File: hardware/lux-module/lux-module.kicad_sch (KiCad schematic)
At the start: 5 parts, among them J1 Conn_01x04, U1 TSL25911FN

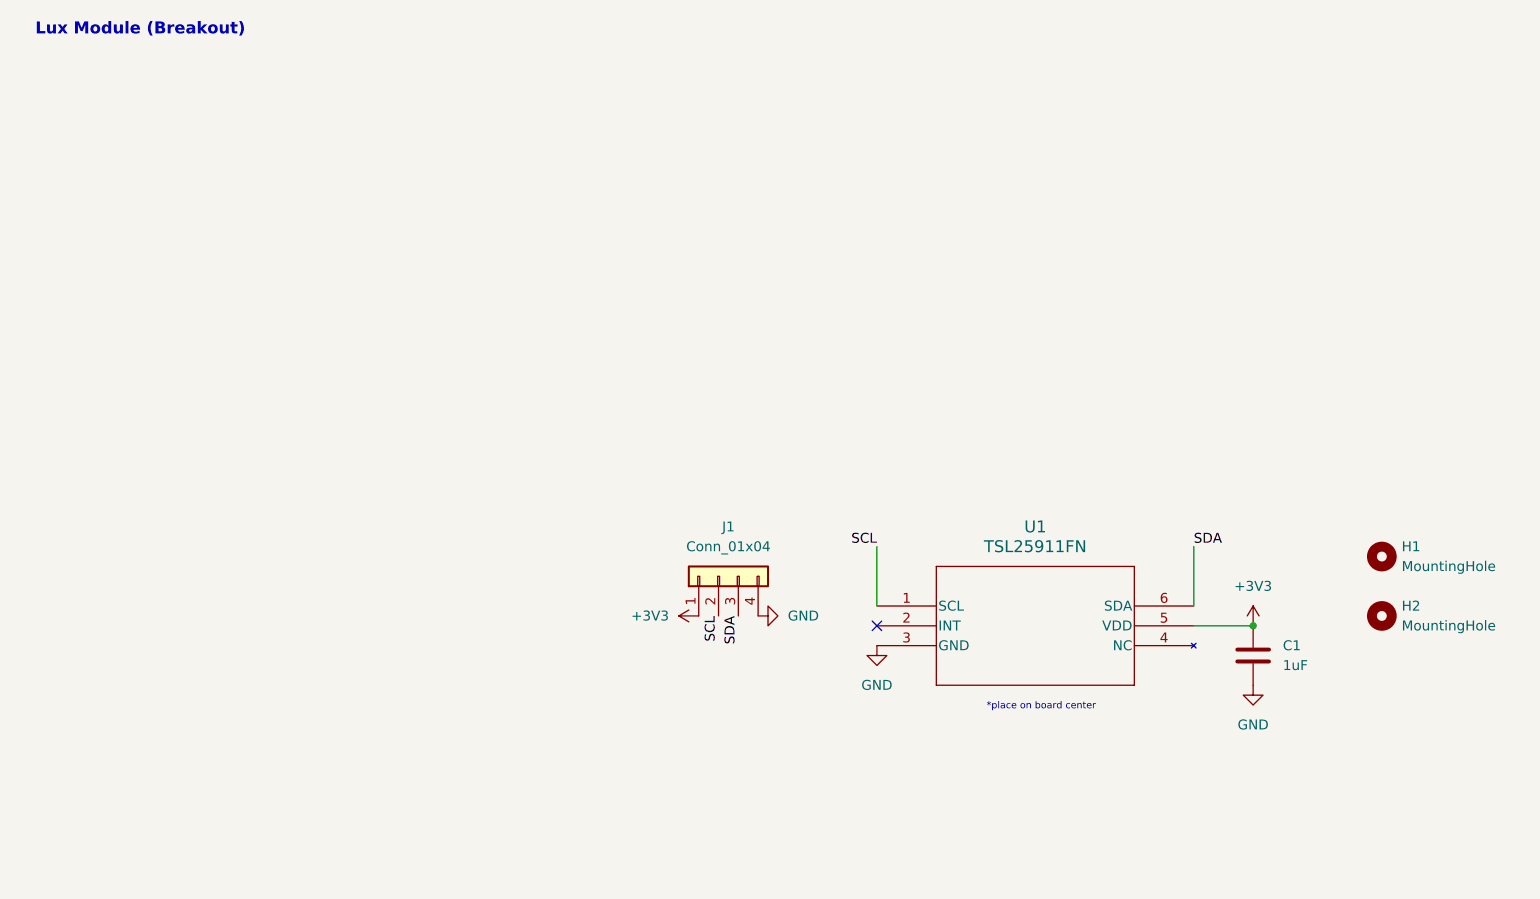
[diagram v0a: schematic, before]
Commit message: finish lux moudle/ALS
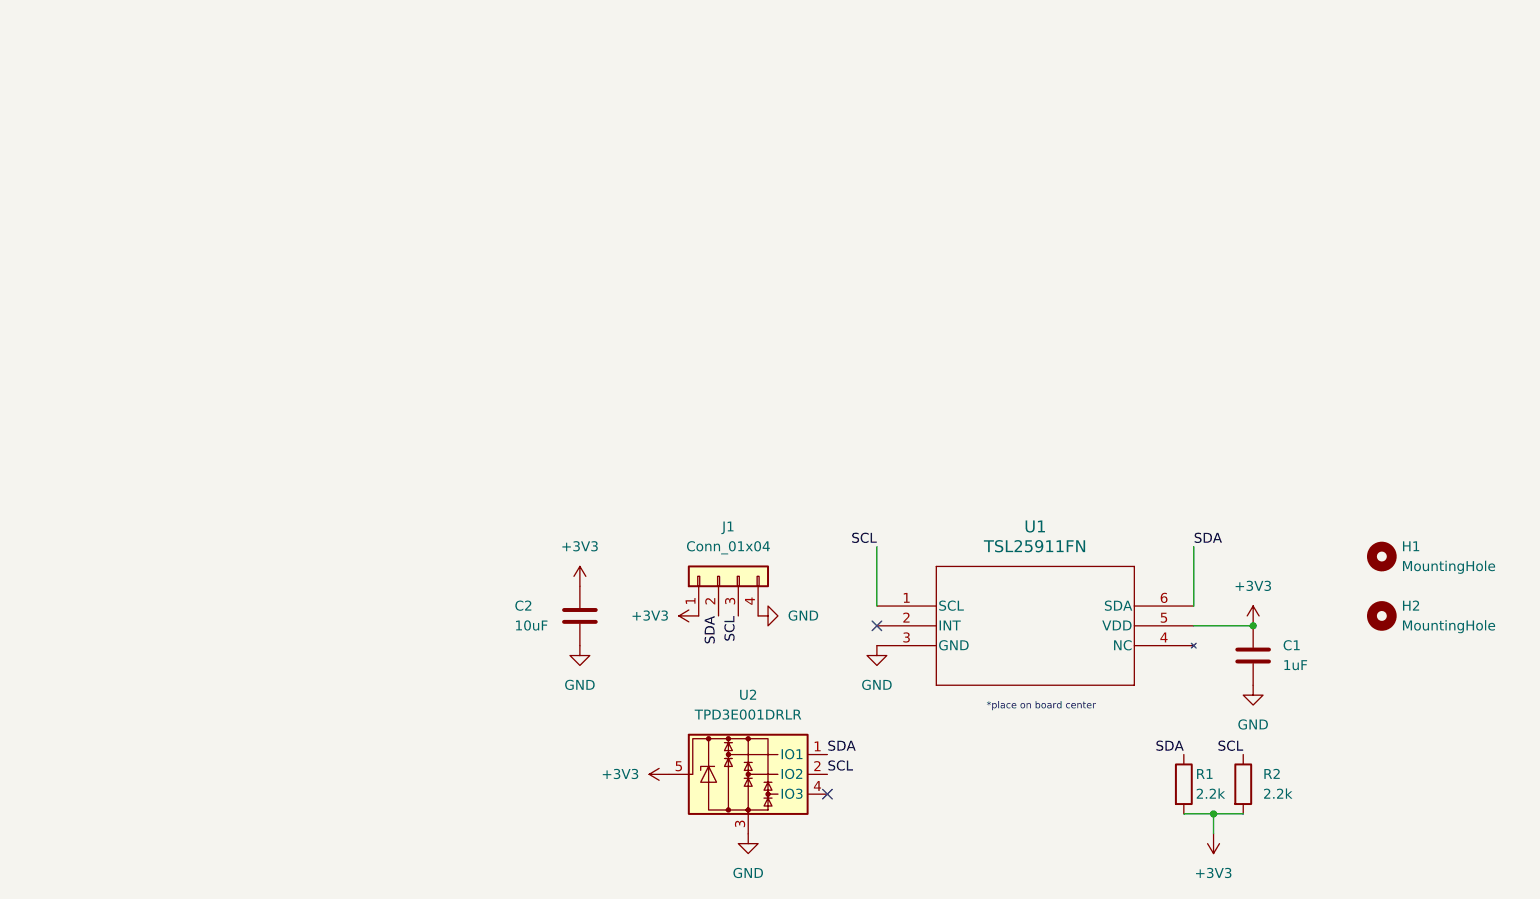
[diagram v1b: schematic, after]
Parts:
- added C2: 10uF, Capacitor_SMD:C_0402_1005Metric, symbol Device:C
- added R1, R2: 2.2k, Resistor_SMD:R_0402_1005Metric, symbol Device:R
- added U2: TPD3E001DRLR, Package_TO_SOT_SMD:SOT-553, symbol Power_Protection:TPD3E001DRLR
- C1: footprint Capacitor_SMD:C_0603_1608Metric -> Capacitor_SMD:C_0402_1005Metric
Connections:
- net +3V3: now also C2.1, R1.2, R2.2, U2.5
- net GND: now also C2.2, U2.3
- net SCL: now also J1.3 (Pin_3), R2.1, U2.2 (IO2); no longer J1.2 (Pin_2)
- net SDA: now also J1.2 (Pin_2), R1.1, U2.1 (IO1); no longer J1.3 (Pin_3)
- no-connect marks 1 -> 2
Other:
- note removed: "Lux Module (Breakout)"

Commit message: W
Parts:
- C1, C2, R1, R2, U1, U2: Purchase (none) -> Yes
- H1, H2: Purchase (none) -> N/A
- J1: Purchase (none) -> No
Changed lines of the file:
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@@
+			)
+		)
+		(property "MPN" ""
+			(at 85.09 96.52 0)
+			(effects
+				(font
+					(size 1.27 1.27)
+				)
+				(hide yes)
+			)
+		)
+		(property "Purchase" "Yes"
+			(at 85.09 96.52 0)
+			(effects
+				(font
+					(size 1.27 1.27)
+				)
+				(hide yes)
 			)
 		)
@@
 			)
 		)
+		(property "MPN" ""
+			(at 171.45 101.6 0)
+			(effects
+				(font
+					(size 1.27 1.27)
+				)
+				(hide yes)
+			)
+		)
+		(property "Purchase" "Yes"
+			(at 171.45 101.6 0)
+			(effects
+				(font
+					(size 1.27 1.27)
+				)
+				(hide yes)
+			)
+		)
 		(pin "2"
 		)
@@
 			)
 		)
+		(property "MPN" ""
+			(at 123.19 95.25 0)
+			(effects
+				(font
+					(size 1.27 1.27)
+				)
+				(hide yes)
+			)
+		)
+		(property "Purchase" "Yes"
+			(at 123.19 95.25 0)
+			(effects
+				(font
+					(size 1.27 1.27)
+				)
+				(hide yes)
+			)
+		)
 		(pin "3"
 		)
@@
 			)
 		)
+		(property "MPN" ""
+			(at 187.96 88.9 0)
+			(effects
+				(font
+					(size 1.27 1.27)
+				)
+				(hide yes)
+			)
+		)
+		(property "Purchase" "N/A"
+			(at 187.96 88.9 0)
+			(effects
+				(font
+					(size 1.27 1.27)
+				)
+				(hide yes)
+			)
+		)
 		(instances
 			(project ""
@@
 			)
 		)
+		(property "MPN" ""
+			(at 162.56 118.11 0)
+			(effects
+				(font
+					(size 1.27 1.27)
+				)
+				(hide yes)
+			)
+		)
+		(property "Purchase" "Yes"
+			(at 162.56 118.11 0)
+			(effects
+				(font
+					(size 1.27 1.27)
+				)
+				(hide yes)
+			)
+		)
 		(pin "1"
 		)
@@
 			)
 		)
+		(property "MPN" ""
+			(at 106.68 116.84 0)
+			(effects
+				(font
+					(size 1.27 1.27)
+				)
+				(hide yes)
+			)
+		)
+		(property "Purchase" "Yes"
+			(at 106.68 116.84 0)
+			(effects
+				(font
+					(size 1.27 1.27)
+				)
+				(hide yes)
+			)
+		)
 		(pin "5"
 		)
@@
 			)
 		)
+		(property "MPN" ""
+			(at 170.18 118.11 0)
+			(effects
+				(font
+					(size 1.27 1.27)
+				)
+				(hide yes)
+			)
+		)
+		(property "Purchase" "Yes"
+			(at 170.18 118.11 0)
+			(effects
+				(font
+					(size 1.27 1.27)
+				)
+				(hide yes)
+			)
+		)
 		(pin "1"
 		)
@@
 			)
 		)
+		(property "MPN" ""
+			(at 102.87 91.44 0)
+			(effects
+				(font
+					(size 1.27 1.27)
+				)
+				(hide yes)
+			)
+		)
+		(property "Purchase" "No"
+			(at 102.87 91.44 0)
+			(effects
+				(font
+					(size 1.27 1.27)
+				)
+				(hide yes)
+			)
+		)
 		(pin "2"
 		)
@@
 			(at 187.96 96.52 0)
 			(effects
+				(font
+					(size 1.27 1.27)
+				)
+				(hide yes)
+			)
+		)
+		(property "MPN" ""
+			(at 187.96 96.52 0)
+			(effects
+				(font
+					(size 1.27 1.27)
+				)
+				(hide yes)
+			)
+		)
+		(property "Purchase" "N/A"
+			(at 187.96 96.52 0)
+			(effects
